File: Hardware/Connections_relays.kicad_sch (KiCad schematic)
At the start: 0 parts

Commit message: Edited schematics
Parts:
- added C14: C, symbol Device:C
- added J1: USB4105-GF-A-120, USB4105-GF-A-120:GCT_USB4105-GF-A-120, symbol USB4105-GF-A-120:USB4105-GF-A-120
- added J2: SD_Card_Device, symbol Connector:SD_Card_Device
- added R2, R3: 5.1k, symbol Device:R
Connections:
- new net: J1.A5 (CC1), R2.2
- new net: J1.B5 (CC2), R3.1
- new net +3.3V: C14.1, J2.4 (VDD)
- new net GND: C14.2, J1.A1_B12 (GND), J1.B1_A12 (GND), J1.SH1 (SHELL_GND), J1.SH2 (SHELL_GND), J1.SH3 (SHELL_GND), J1.SH4 (SHELL_GND), J2.3 (VSS), J2.6 (VSS), R2.1, R3.2
- new net SDIO_CLK: J2.5 (CLK)
- new net SDIO_CMD: J2.2 (CMD)
- new net SDIO_D0: J2.7 (DAT0)
- new net SDIO_D1: J2.8 (DAT1)
- new net SDIO_D2: J2.9 (DAT2)
- new net SDIO_D3: J2.1 (CD/DAT3)
- new net USB_D+: J1.A6 (DP1), J1.B6 (DP2)
- new net USB_D-: J1.A7 (DN1), J1.B7 (DN2)
- new net VBUS: J1.A4_B9 (VBUS), J1.B4_A9 (VBUS)
- no-connect marks 0 -> 2
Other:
- note added: "SD-card"
- note added: "TODO: -Add pull up resisors on SDIO lines -Add series resistors"
- note added: "USB-c Connector"
- company: (none) -> Burocket
- title: (none) -> Connections & Relays

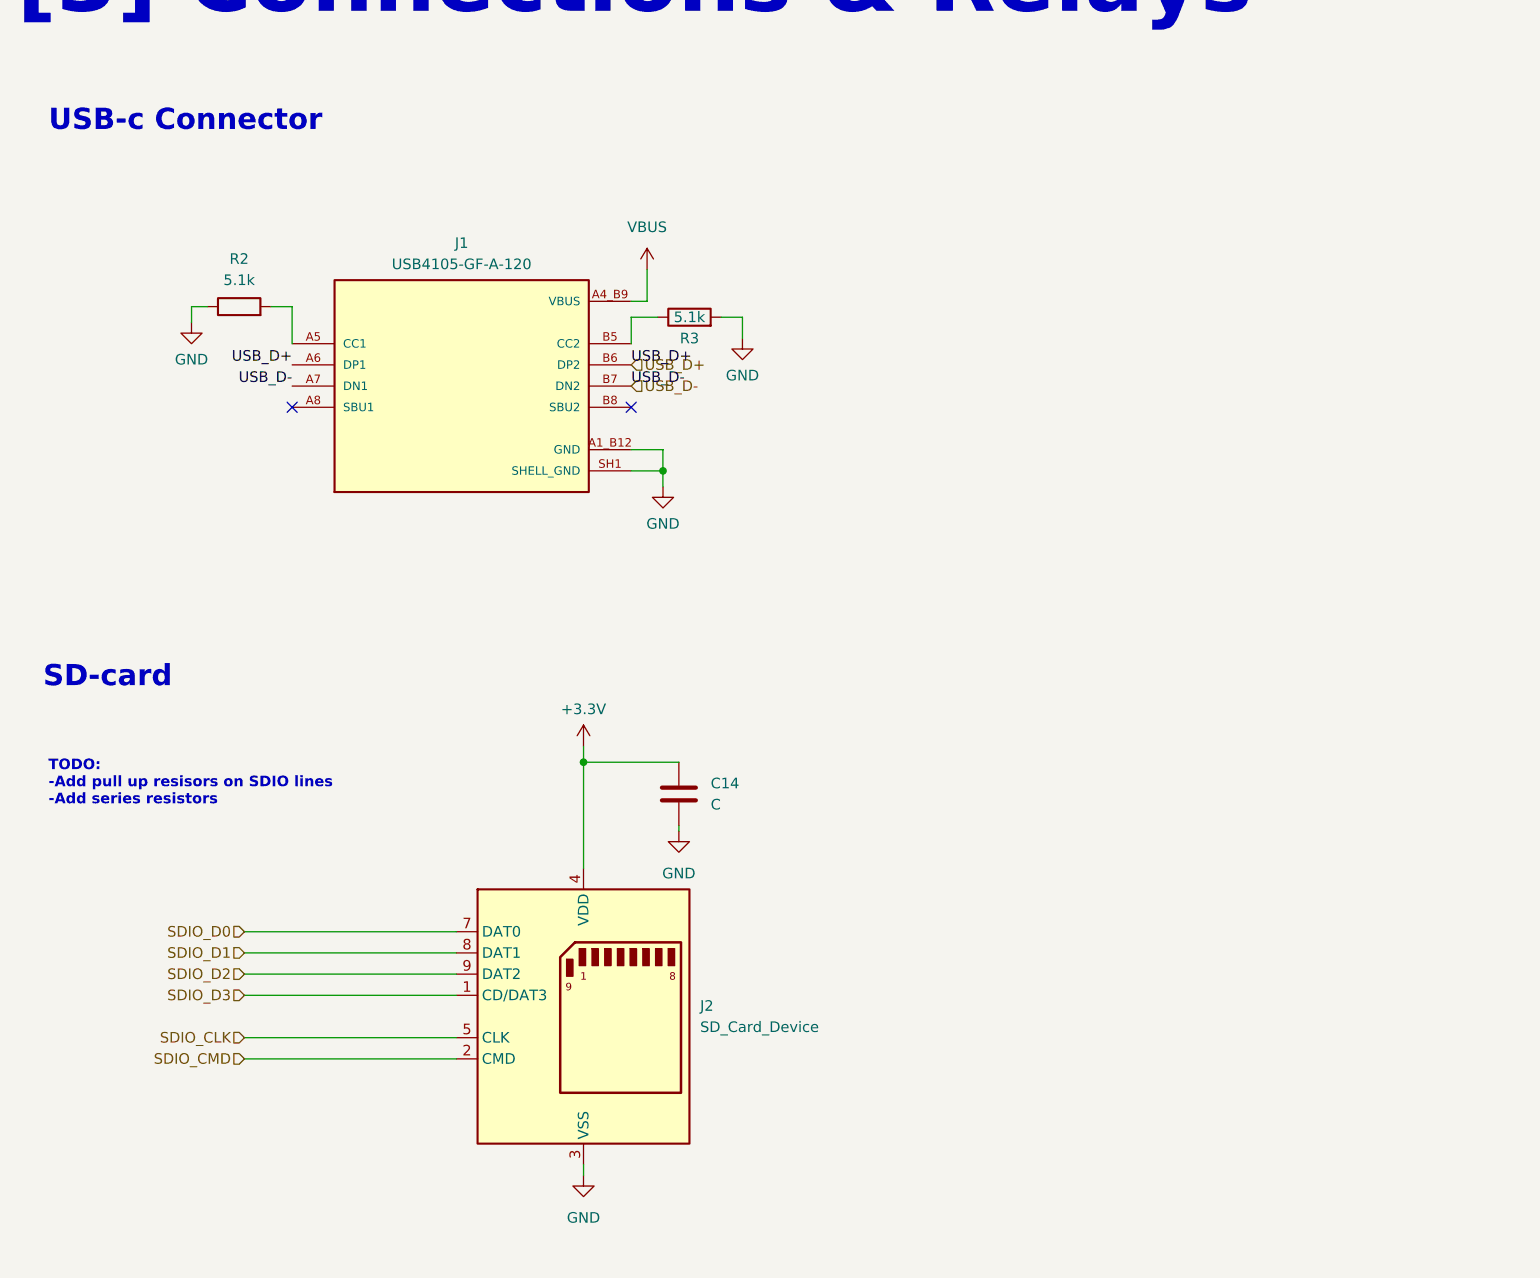
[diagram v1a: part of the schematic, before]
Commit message: Selected components and added their properties, started the power schematics
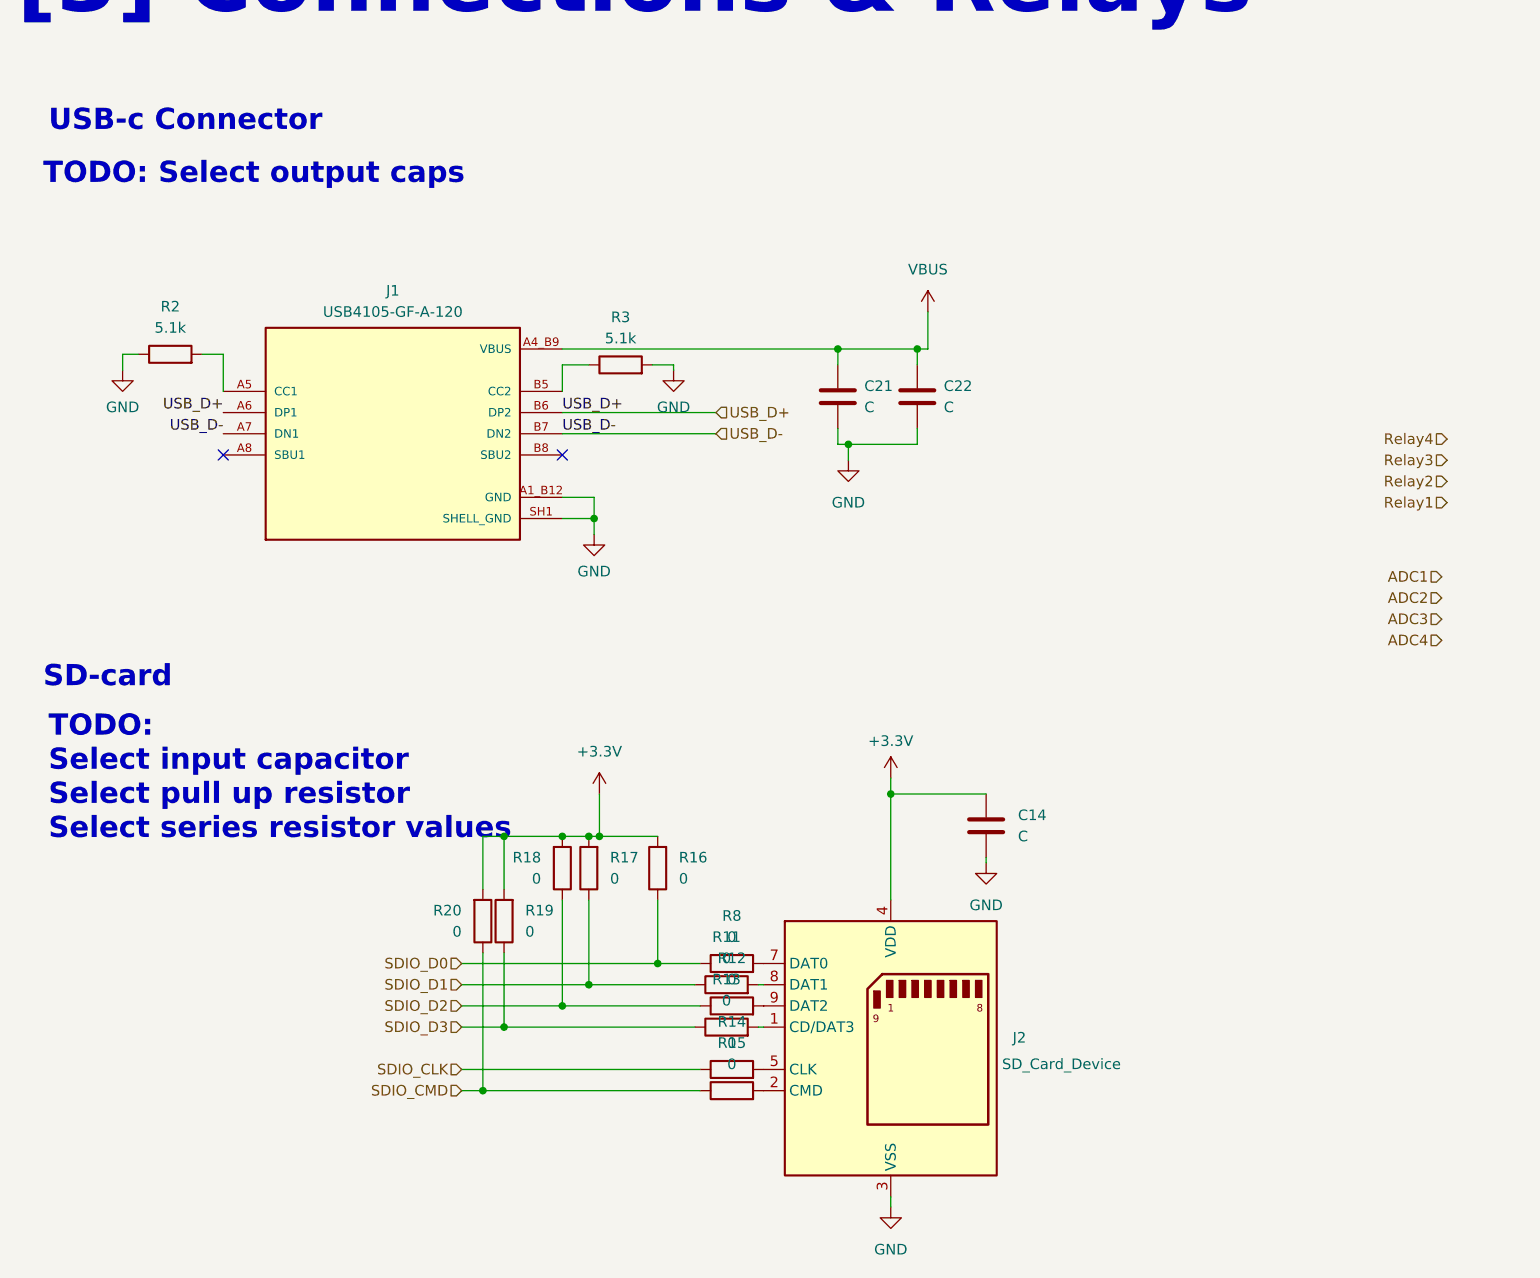
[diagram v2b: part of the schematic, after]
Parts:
- added C21, C22: C, symbol Device:C
- added R11, R12, R13, R14, R15, R16, R17, R18, R19, R20, R8: 0, symbol Device:R
- J2: footprint (none) -> footprints.ul_473521001:CON00878_8_MOL; Distributer Link (none) -> https://www.ozdisan.com/p/pc-kart-soketleri-706/molex-molex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; Part number (none) -> MOLEX-473521001
- R2, R3: footprint (none) -> Resistor_SMD:R_0402_1005Metric; Distributer Link (none) -> https://www.ozdisan.com/p/smt-smd-ve-cip-direncler-194/pana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; Part Number (none) -> ERJ2RKF5101X
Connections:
- net +3.3V: now also R16.2, R17.2, R18.2, R19.2, R20.2
- net GND: now also C21.2, C22.2
- net SDIO_CLK: now also R14.1; no longer J2.5 (CLK)
- net SDIO_CMD: now also R15.1, R20.1; no longer J2.2 (CMD)
- net SDIO_D0: now also R16.1, R8.1; no longer J2.7 (DAT0)
- net SDIO_D1: now also R11.1, R17.1; no longer J2.8 (DAT1)
- net SDIO_D2: now also R12.1, R18.1; no longer J2.9 (DAT2)
- net SDIO_D3: now also R13.1, R19.1; no longer J2.1 (CD/DAT3)
- net VBUS: now also C21.1, C22.1
- new net: J2.9 (DAT2), R12.2
- new net: J2.5 (CLK), R14.2
- new net: J2.1 (CD/DAT3), R13.2
- new net: J2.8 (DAT1), R11.2
- new net: J2.7 (DAT0), R8.2
- new net: J2.2 (CMD), R15.2
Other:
- note added: "TODO: Select input capacitor Select pull up resistor Select series resistor values"
- note added: "TODO: Select output caps"
- note removed: "TODO: -Add pull up resisors on SDIO lines -Add series resistors"
- moved on the sheet: C14, J1, J2, R2

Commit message: Added a simulations file, added App Notes file, Finalized SD-card design type shit
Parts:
- removed J2: SD_Card_Device, footprints.ul_473521001:CON00878_8_MOL, symbol Connector:SD_Card_Device
- added C27: 2.2uF, Capacitor_SMD:C_0402_1005Metric, symbol Device:C
- added C28, C29, C30, C31, C32: 100nF, Capacitor_SMD:C_0402_1005Metric, symbol Device:C
- added D3: ESD321DYAR, Diode_SMD:D_SOD-523, symbol Diode:ESD5Zxx
- added D4: Green LED, LED_SMD:LED_0603_1608Metric, symbol Device:LED
- added J3: 1040310811, Molex 1040310811:104031-0811_MOL, symbol 2026-07-10_16-12-29:1040310811
- added R25: 1k, Resistor_SMD:R_0402_1005Metric, symbol Device:R
- added U4: TPD2EUSB30DRTR, Package_TO_SOT_SMD:Texas_DRT-3, symbol Power_Protection:TPD2EUSB30A
- C14: value C -> 10uF; footprint (none) -> Capacitor_SMD:C_0603_1608Metric; Distributer Link (none) -> https://www.ozdisan.com/p/smt-smd-ve-mlcc-kapasitorler-184/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; Part Number (none) -> GRT188C81C106ME13D
- C21: value C -> 2.2uF; footprint (none) -> Capacitor_SMD:C_0402_1005Metric; Distributer Link (none) -> http://ozdisan.com/p/smt-smd-ve-mlcc-kapasitorler-184/murat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; Part Number (none) -> GRT155C81A225ME13D
- C22: value C -> 100nF; footprint (none) -> Capacitor_SMD:C_0402_1005Metric; Distributer Link (none) -> https://www.ozdisan.com/p/smt-smd-ve-mlcc-kapasitorler-184/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; Part Number (none) -> GRT155R71E104KE01D
- R14: value 0 -> 22; footprint (none) -> Resistor_SMD:R_0402_1005Metric; Distributer Link (none) -> https://www.ozdisan.com/p/smt-smd-ve-cip-direncler-194/pana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; Part Number (none) -> ERJ2RKF22R0X
- R16, R17, R18, R19, R20, R8: value 0 -> 10k; footprint (none) -> Resistor_SMD:R_0603_1608Metric; Distributer Link (none) -> https://www.ozdisan.com/p/smt-smd-ve-cip-direncler-194/pana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; Part Number (none) -> ERJ3EKF1002V
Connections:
- net +3.3V: now also R16.1, R17.1, R18.1, R19.1, R20.1, R8.1, C27.1, J3.4 (VDD); no longer R16.2, R17.2, R18.2, R19.2, R20.2
- net ADC1: now also R11.1, C29.1
- net ADC2: now also R12.1, C30.1
- net ADC3: now also R13.1, C31.1
- net ADC4: now also R15.1, C32.1
- net GND: now also C27.2, C28.2, C29.2, C30.2, C31.2, C32.2, D3.2 (A), D4.1 (K), J3.6 (VSS), J3.9 (SW_DETECT), U4.3 (GND)
- net SDIO_CMD: now also R18.2, J3.3 (CMD); no longer R15.1, R20.1
- net SDIO_D0: now also R16.2, J3.7 (DAT0); no longer R16.1, R8.1
- net SDIO_D1: now also R20.2, J3.8 (DAT1); no longer R11.1, R17.1
- net SDIO_D2: now also R19.2, J3.1 (DAT2); no longer R12.1, R18.1
- net SDIO_D3: now also R17.2, J3.2 (CD/DAT3); no longer R13.1, R19.1
- net USB_D+: now also U4.1 (D+)
- net USB_D-: now also U4.2 (D-)
- net VBUS: now also D3.1 (K), R25.1
- net at R14.2: now also J3.5 (CLK)
- net SDIO_CDS: now reaches R8.2
- net SDIO_CDS: now also C28.1, J3.10 (SW_DETECT)
- new net: D4.2 (A), R25.2
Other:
- note removed: "TODO: Select input capacitor Select pull up resistor Select series resistor values"
- note removed: "TODO: Select output caps"
- moved on the sheet: C14, J1, R14, R2, R3

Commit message: +1000 Aura
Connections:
- net SDIO_CLK: now also R14.2; no longer R14.1
- net at J3.5 (CLK): now also R14.1; no longer R14.2
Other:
- moved on the sheet: C14, C27, C28, C29, C30, C31, C32, J3, R11, R12, R13, R14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

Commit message: Only SSR and ferrite bead selection is left
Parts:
- removed C14: 10uF, Capacitor_SMD:C_0603_1608Metric, symbol Device:C
- removed C30, C31, C32: 100nF, Capacitor_SMD:C_0402_1005Metric, symbol Device:C
- removed R11: 0, symbol Device:R
- added C36, C37, C39: 100nF, Capacitor_SMD:C_0402_1005Metric, symbol Device:C
- added C46: 22uF, Capacitor_SMD:C_0805_2012Metric, symbol Device:C
- added J2, J4, J6, J7: Conn_01x02, symbol Connector_Generic:Conn_01x02
- added Q2, Q3, Q4, Q5: NMOS, symbol Simulation_SPICE:NMOS
- added R33, R34, R39, R40, R42, R43, R45, R46, R47, R48, R49, R50, R51: R, symbol Device:R
- added R35, R41, R44, R52: 4.7, Resistor_SMD:R_0402_1005Metric, symbol Device:R
- R12, R13, R15: value 0 -> R
- R16, R17, R18, R19, R20: footprint Resistor_SMD:R_0603_1608Metric -> Resistor_SMD:R_0402_1005Metric; Distributer Link https://www.ozdisan.com/p/smt-smd-ve-cip-direncler-194/pana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 -> https://www.ozdisan.com/p/smt-smd-ve-cip-direncler-194/roya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; Part Number ERJ3EKF1002V -> CQ02WGF1002TCE
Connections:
- net +3.3V: now also C46.1
- net ADC1: now also R52.1
- net ADC2: now also C36.1, R35.1; no longer R12.1
- net ADC3: now also C39.1, R44.1; no longer R13.1
- net ADC4: now also C37.1, R41.1; no longer R15.1
- net GND: now also R13.2, C36.2, C37.2, C39.2, C46.2, Q2.3 (S), Q3.3 (S), Q4.3 (S), Q5.3 (S), R33.2, R40.2, R43.2, R46.2, R47.2, R49.2, R51.2
- net Relay1: now also R34.1
- net Relay2: now also R39.1
- net Relay3: now also R45.1
- net Relay4: now also R42.1
- net SDIO_CMD: now also R19.2; no longer R18.2
- net SDIO_D0: now also R20.2; no longer R16.2
- net SDIO_D1: now also R16.2; no longer R20.2
- net SDIO_D2: now also R17.2; no longer R19.2
- net SDIO_D3: now also R18.2; no longer R17.2
- net at R12.2: now also R13.1, R41.2
- net at R15.2: now also R44.2, R47.1
- new net: J7.2 (Pin_2), Q5.1 (D), R15.1
- new net: Q5.2 (G), R45.2, R46.1
- new net: Q4.2 (G), R42.2, R43.1
- new net: Q3.2 (G), R39.2, R40.1
- new net: R35.2, R48.2, R49.1
- new net: Q2.2 (G), R33.1, R34.2
- new net: R50.2, R51.1, R52.2
- new net: J6.2 (Pin_2), Q4.1 (D), R12.1
- new net: J4.2 (Pin_2), Q3.1 (D), R48.1
- new net: J2.2 (Pin_2), Q2.1 (D), R50.1
- new net +BATT: J2.1 (Pin_1), J4.1 (Pin_1), J6.1 (Pin_1), J7.1 (Pin_1)
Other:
- note added: "70-ohm impedance matching"
- note added: "MAX Current consumption ≈ 163mA"
- note added: "Relay-1"
- note added: "Relay-2"
- note added: "Relay-3"
- note added: "Relay-4"
- note added: "Select gate resistors so that: - Rise and fall time are small so low power dissipation on mosfet - try to achieve critically damped oscillation caused by parasitic inductance and capacitance"
- moved on the sheet: C21, C22, C27, C28, C29, D3, D4, J1, J3, R14, R2, R25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

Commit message: Changed some stupid mistake -100 Aura
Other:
- note added: "90-ohm impedance matching"
- note removed: "70-ohm impedance matching"

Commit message: Ne yazacagimi bilemedim
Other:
- moved on the sheet: C29, J2, Q2, R33, R34, R50, R51, R52

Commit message: Commit bulamadim :)
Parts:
- removed R8: 10k, Resistor_SMD:R_0603_1608Metric, symbol Device:R
- added C15: 100nF, Capacitor_SMD:C_0402_1005Metric, symbol Device:C
- added C47: 22uF, Capacitor_SMD:C_0805_2012Metric, symbol Device:C
- added R62, R64: 10k, Resistor_SMD:R_0402_1005Metric, symbol Device:R
- added R63: 22Ω, Resistor_SMD:R_0402_1005Metric, symbol Device:R
- added R66: 28k, Resistor_SMD:R_0402_1005Metric, symbol Device:R
- added U11: W25Q128JVS, Package_SO:SOIC-8_5.3x5.3mm_P1.27mm, symbol Memory_Flash:W25Q128JVS
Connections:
- net +3.3V: now also C15.1, C47.1, R62.1, R64.1, R66.1, U11.3 (~{WP}/IO_{2}), U11.8 (VCC)
- net GND: now also C15.2, C47.2, U11.4 (GND)
- net SDIO_CDS: now also R66.2
- new net: R63.1, U11.6 (CLK)
- new net: R64.2, U11.7 (~{HOLD}/~{RESET}/IO_{3})
- new net BARO_MISO: U11.2 (DO/IO_{1})
- new net BARO_MOSI: U11.5 (DI/IO_{0})
- new net BARO_SCK: R63.2
- new net Flash_SS: R62.2, U11.1 (~{CS})
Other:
- note added: "Flash Memory"
- moved on the sheet: C21, C22, C27, C28, C29, C36, C37, C39, C46, D3, D4, J1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
